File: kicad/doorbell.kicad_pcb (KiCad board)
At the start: 4 copper layers, 52.5 x 60.2 mm, 67 parts, among them J1 USB-C (USB4105), J2 WF26 (6-way screw), K1 G6K-2F-Y 4.5V, K2 G6K-2F-Y 4.5V, K3 G6K-2F-Y 4.5V, Q1 2N7002, Q2 2N7002, Q3 2N7002, SW1 BOOT, SW2 EN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

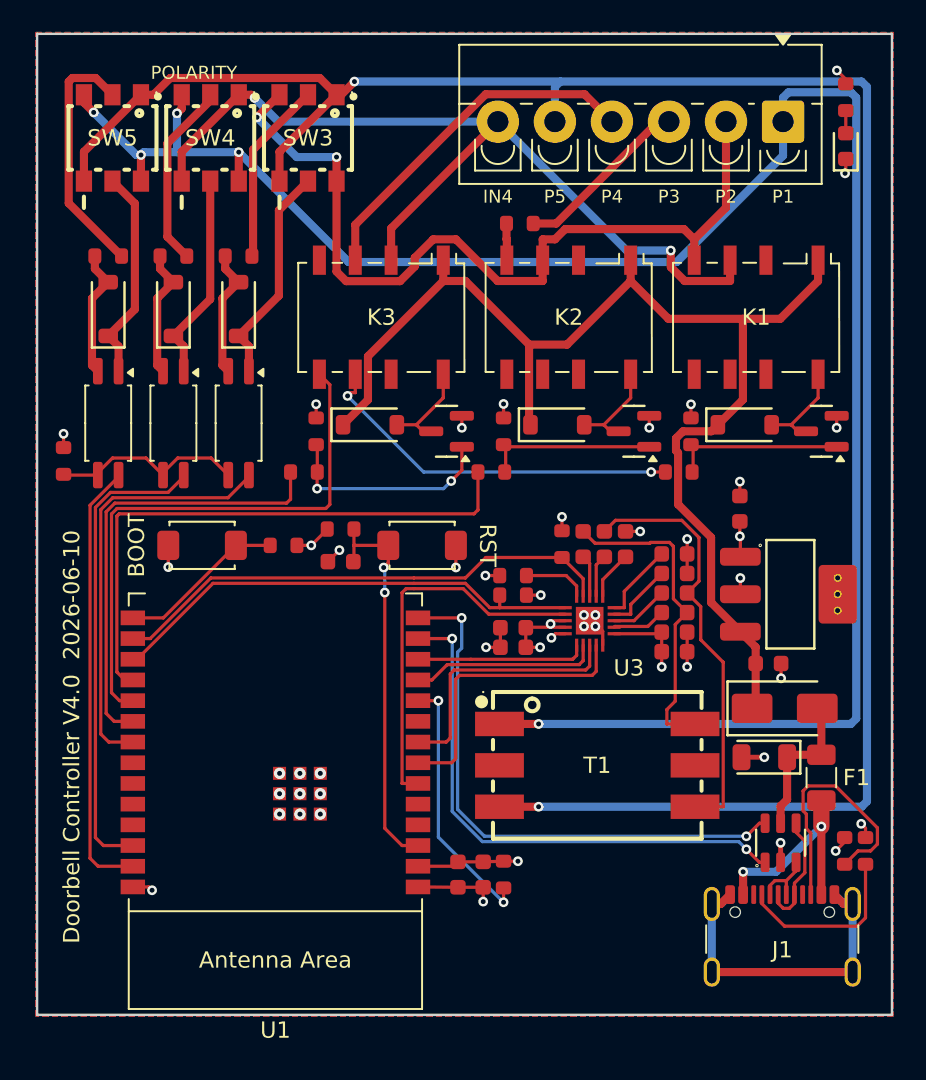
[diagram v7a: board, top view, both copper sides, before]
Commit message: Hand-route power nets
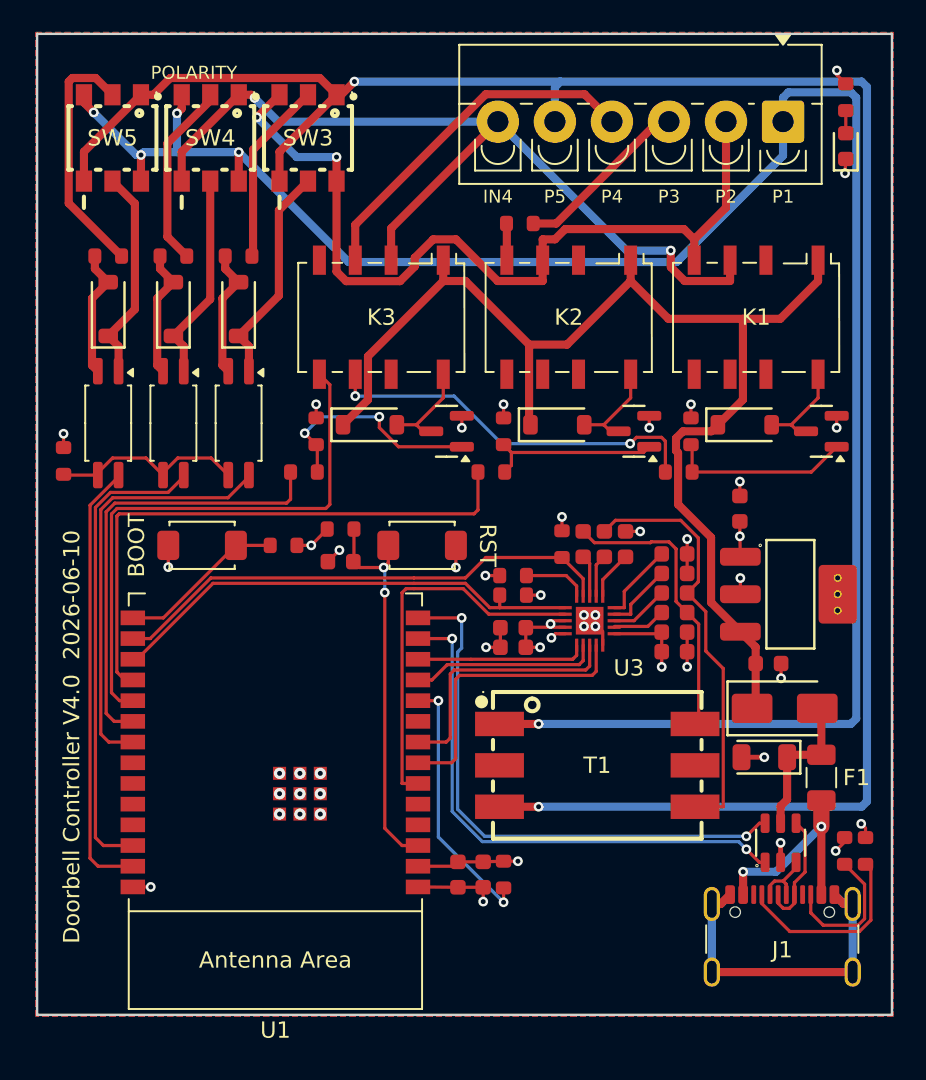
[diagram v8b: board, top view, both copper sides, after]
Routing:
- net USB_CC2: track 15.8 -> 8.75 mm
- net SEC_A: track 19.5 -> 17.6 mm
- net USB_CC1: track 11.0 -> 11.8 mm
- net GND: track 57.4 -> 58.1 mm
- net GATE1: track 10.6 -> 11.2 mm
- net GATE1_PRE: track 23.1 -> 23.7 mm
